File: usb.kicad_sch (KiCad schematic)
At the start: 11 parts, among them J3 USB_C_Receptacle_USB2.0_16P, U8 USBLC6-2SC6, U9 CP2102N-Axx-xQFN24

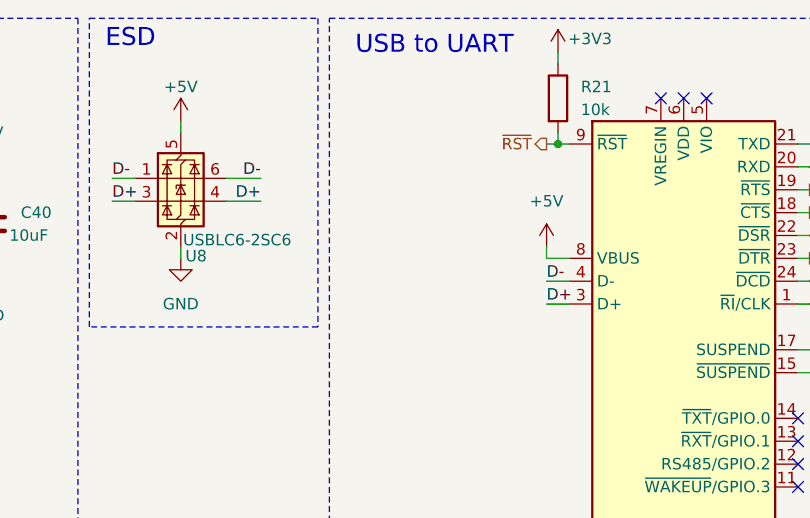
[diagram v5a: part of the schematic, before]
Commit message: added test points to uart
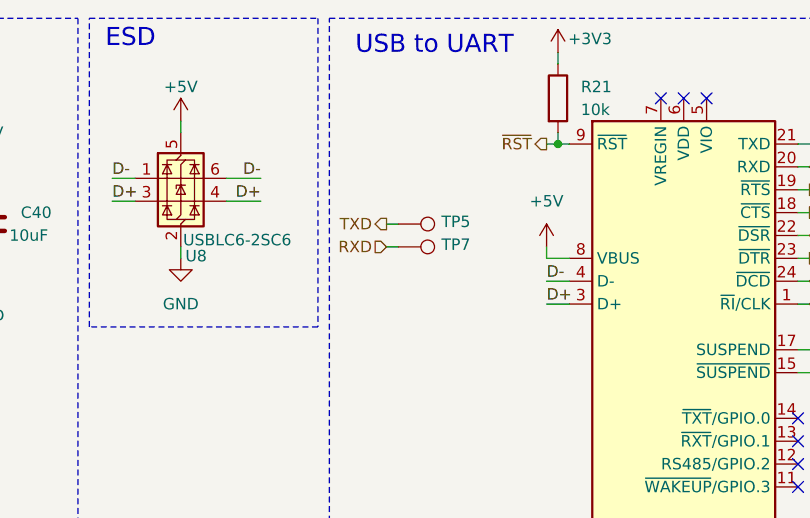
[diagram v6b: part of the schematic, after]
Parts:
- added TP5, TP7: TestPoint, TestPoint:TestPoint_Pad_D1.0mm, symbol Connector:TestPoint
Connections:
- net RXD: now also TP7.1
- net TXD: now also TP5.1
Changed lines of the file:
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@@
+	(wire
+		(pts
+			(xy 109.22 38.1) (xy 110.49 38.1)
+		)
+		(stroke
+			(width 0)
+			(type default)
+		)
+	)
 	(wire
 		(pts
@@
 		(pts
 			(xy 30.48 69.85) (xy 30.48 68.58)
+		)
+		(stroke
+			(width 0)
+			(type default)
+		)
+	)
+	(wire
+		(pts
+			(xy 109.22 35.56) (xy 110.49 35.56)
 		)
 		(stroke
@@
 	(hierarchical_label "RXD"
 		(shape input)
+		(at 109.22 38.1 180)
+		(effects
+			(font
+				(size 1.27 1.27)
+			)
+			(justify right)
+		)
+	)
+	(hierarchical_label "RXD"
+		(shape input)
 		(at 156.21 29.21 0)
 		(effects
@@
 			)
 			(justify left)
+		)
+	)
+	(hierarchical_label "TXD"
+		(shape output)
+		(at 109.22 35.56 180)
+		(effects
+			(font
+				(size 1.27 1.27)
+			)
+			(justify right)
 		)
 	)
@@
 	)
 	(symbol
+		(lib_id "Connector:TestPoint")
+		(at 110.49 38.1 270)
+		(unit 1)
+		(exclude_from_sim no)
+		(in_bom yes)
+		(on_board yes)
+		(dnp no)
+		(property "Reference" "TP7"
+			(at 115.316 37.846 90)
+			(effects
+				(font
+					(size 1.27 1.27)
+				)
+				(justify left)
+			)
+		)
+		(property "Value" "TestPoint"
+			(at 112.5221 40.64 0)
+			(effects
+				(font
+					(size 1.27 1.27)
+				)
+				(justify left)
+				(hide yes)
+			)
+		)
+		(property "Footprint" "TestPoint:TestPoint_Pad_D1.0mm"
+			(at 110.49 43.18 0)
+			(effects
+				(font
+					(size 1.27 1.27)
+				)
+				(hide yes)
+			)
+		)
+		(property "Datasheet" "~"
+			(at 110.49 43.18 0)
+			(effects
+				(font
+					(size 1.27 1.27)
+				)
+				(hide yes)
+			)
+		)
+		(property "Description" "test point"
+			(at 110.49 38.1 0)
+			(effects
+				(font
+					(size 1.27 1.27)
+				)
+				(hide yes)
+			)
+		)
+		(pin "1"
+		)
+		(instances
+			(project "meko-pcb"
+				(path "/bdd43acd-23c1-472b-909a-8e24eb60d56d/f706aad0-fe72-4f1f-8f4a-da2e99c9f80e"
+					(reference "TP7")
+					(unit 1)
+				)
+			)
+		)
+	)
+	(symbol
 		(lib_id "Interface_USB:CP2102N-Axx-xQFN24")
 		(at 142.24 49.53 0)
@@
 					(unit 1)
 				)
+			)
+		)
+	)
+	(symbol
+		(lib_id "Connector:TestPoint")
+		(at 110.49 35.56 270)
+		(unit 1)
+		(exclude_from_sim no)
+		(in_bom yes)
+		(on_board yes)
+		(dnp no)
+		(property "Reference" "TP5"
+			(at 115.316 35.306 90)
+			(effects
+				(font
+					(size 1.27 1.27)
+				)
+				(justify left)
+			)
+		)
+		(property "Value" "TestPoint"
+			(at 112.5221 38.1 0)
+			(effects
+				(font
+					(size 1.27 1.27)
+				)
+				(justify left)
+				(hide yes)
+			)
+		)
+		(property "Footprint" "TestPoint:TestPoint_Pad_D1.0mm"
+			(at 110.49 40.64 0)
+			(effects
+				(font
+					(size 1.27 1.27)
+				)
+				(hide yes)
+			)
+		)
+		(property "Datasheet" "~"
+			(at 110.49 40.64 0)
+			(effects
+				(font
+					(size 1.27 1.27)
+				)
+				(hide yes)
+			)
+		)
+		(property "Description" "test point"
+			(at 110.49 35.56 0)
+			(effects
+				(font
+					(size 1.27 1.27)
+				)
+				(hide yes)
+			)
+		)
+		(pin "1"
+		)
+		(instances
+			(project "meko-pcb"
+				(path "/bdd43acd-23c1-472b-909a-8e24eb60d56d/f706aad0-fe72-4f1f-8f4a-da2e99c9f80e"
+					(reference "TP5")
+					(unit 1)
+				)
